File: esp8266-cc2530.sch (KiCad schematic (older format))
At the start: 34 parts, among them J1 CC2530_programmingHeader, U1 WeMos_D1_mini, U2 AMS1117-3.3, U3 CC2530Fxxx, U4 RFX2401C, Y1 32.768kHz, Y2 32MHz

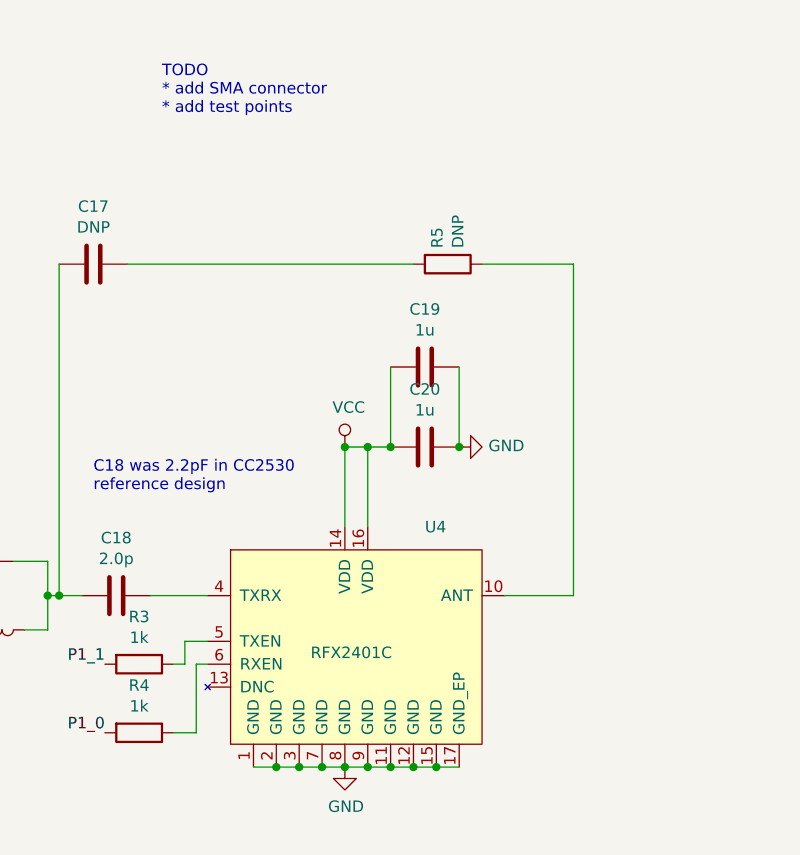
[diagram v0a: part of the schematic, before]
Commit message: added sma connector
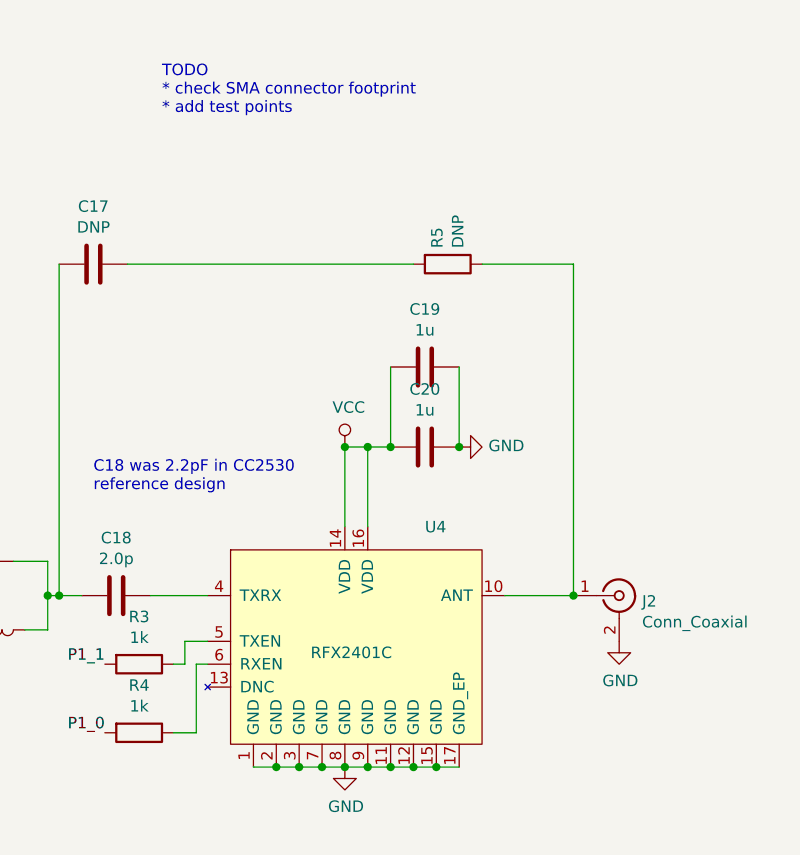
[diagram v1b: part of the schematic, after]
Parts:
- added J2: Conn_Coaxial, Connector_Coaxial:SMA_Amphenol_132289_EdgeMount, symbol Connector:Conn_Coaxial
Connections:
- net GND: now also J2.2 (Ext)
- net at R5.1, U4.10 (ANT): now also J2.1 (In)
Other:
- note added: "TODO\n* check SMA connector footprint\n* add test points"
- note removed: "TODO\n* add SMA connector\n* add test points"
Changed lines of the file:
@@
 Connection ~ 9800 2400
 Text Notes 8500 950  0    50   ~ 0
-TODO\n* add SMA connector\n* add test points
+TODO\n* check SMA connector footprint\n* add test points
 $Comp
 L Device:C C3
@@
 Text Notes 8200 2600 0    50   ~ 0
 C18 was 2.2pF in CC2530 \nreference design
+$Comp
+L Connector:Conn_Coaxial J2
+U 1 1 5ED9BD71
+P 10500 3050
+F 0 "J2" H 10600 3025 50  0000 L CNN
+F 1 "Conn_Coaxial" H 10600 2934 50  0000 L CNN
+F 2 "Connector_Coaxial:SMA_Amphenol_132289_EdgeMount" H 10500 3050 50  0001 C CNN
+F 3 " ~" H 10500 3050 50  0001 C CNN
+	1    10500 3050
+	1    0    0    -1
+$EndComp
+Connection ~ 10300 3050
+$Comp
+L power:GND #PWR0120
+U 1 1 5ED9D9C1
+P 10500 3250
+F 0 "#PWR0120" H 10500 3000 50  0001 C CNN
+F 1 "GND" H 10505 3077 50  0000 C CNN
+F 2 "" H 10500 3250 50  0001 C CNN
+F 3 "" H 10500 3250 50  0001 C CNN
+	1    10500 3250
+	1    0    0    -1
+$EndComp
 $EndSCHEMATC

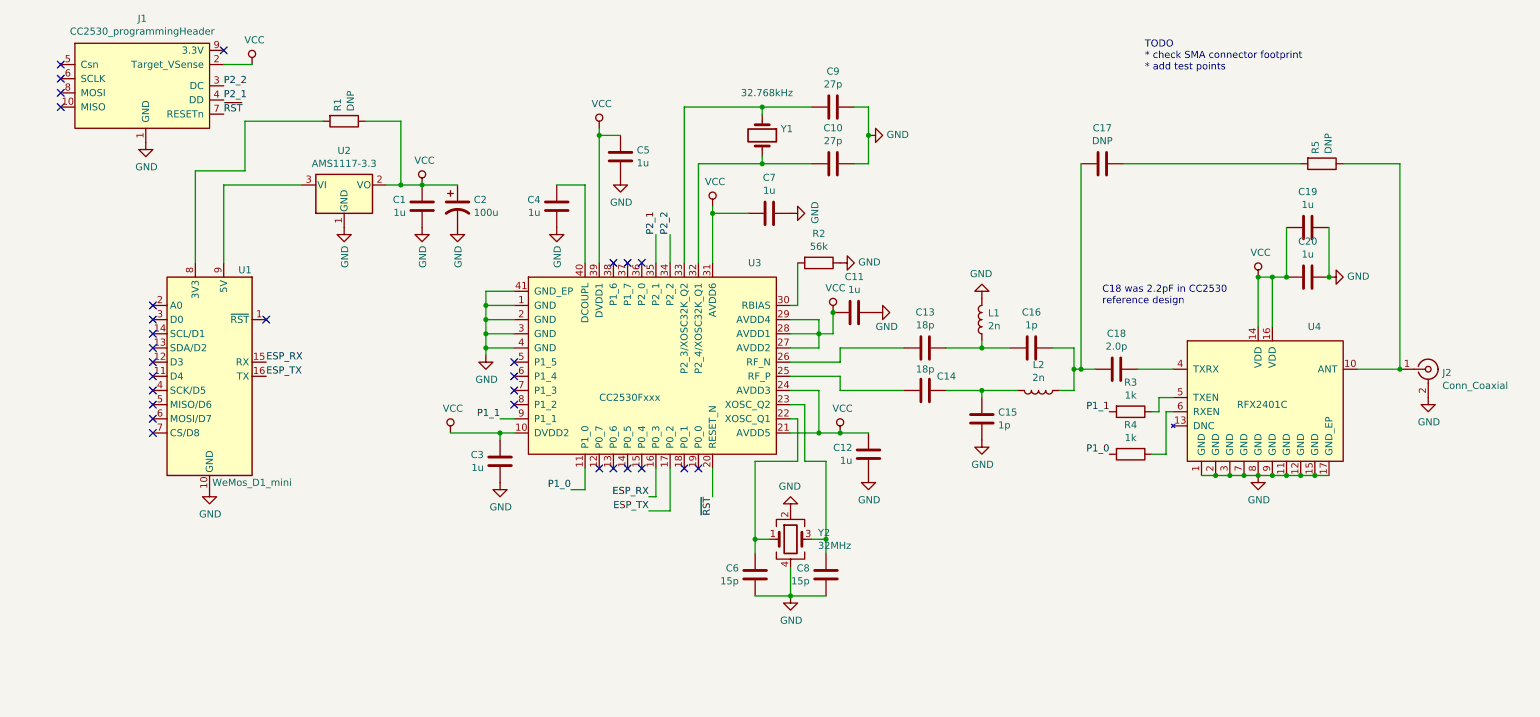
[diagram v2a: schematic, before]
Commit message: removed RFX2401 bypass, added DNP to power CC2530 from debugger
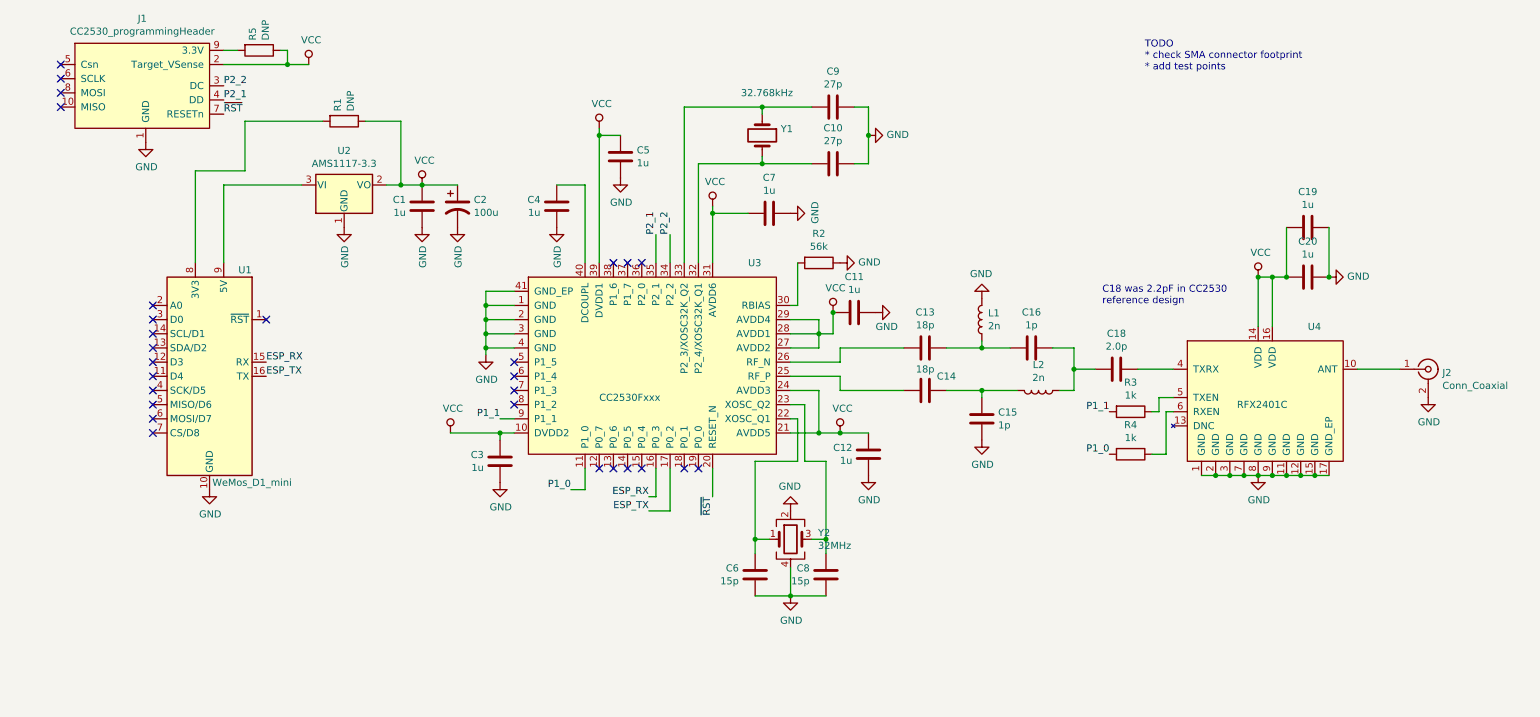
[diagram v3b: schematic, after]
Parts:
- removed C17: DNP, Capacitor_SMD:C_0805_2012Metric, symbol Device:C
- J1: footprint Connector_PinHeader_2.54mm:PinHeader_2x05_P2.54mm_Vertical_SMD -> Connector_PinHeader_1.27mm:PinHeader_2x05_P1.27mm_Vertical_SMD
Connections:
- net VCC: now also R5.1
- net at J2.1 (In), U4.10 (ANT): no longer R5.1
- net at R5.2: now also J1.9 (3.3V)
- no-connect marks 29 -> 28
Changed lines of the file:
@@
 Text Label 5000 3950 2    50   ~ 0
 ESP_RX
-$Comp
-L Device:C C17
-U 1 1 5EB635D2
-P 8200 1600
-F 0 "C17" V 7948 1600 50  0000 C CNN
-F 1 "DNP" V 8039 1600 50  0000 C CNN
-F 2 "Capacitor_SMD:C_0805_2012Metric" H 8238 1450 50  0001 C CNN
-F 3 "~" H 8200 1600 50  0001 C CNN
-	1    8200 1600
-	0    -1   1    0
-$EndComp
-$Comp
-L Device:R R5
-U 1 1 5EB77ED4
-P 9750 1600
-F 0 "R5" H 9680 1554 50  0000 R CNN
-F 1 "DNP" H 9680 1645 50  0000 R CNN
-F 2 "Resistor_SMD:R_0805_2012Metric" V 9680 1600 50  0001 C CNN
-F 3 "~" H 9750 1600 50  0001 C CNN
-	1    9750 1600
-	0    1    1    0
-$EndComp
 Text Label 8250 3350 2    50   ~ 0
 P1_1
 Text Label 8250 3650 2    50   ~ 0
 P1_0
-Wire Wire Line
-	9900 1600 10300 1600
-Wire Wire Line
-	8350 1600 9600 1600
-Wire Wire Line
-	8000 3050 8050 3050
-Wire Wire Line
-	10300 1600 10300 3050
-Wire Wire Line
-	8050 1600 8050 3050
-Connection ~ 8050 3050
-Wire Wire Line
-	8050 3050 8150 3050
 $Comp
 L power:GND #PWR0129
@@
 F 0 "J1" H 1425 1325 50  0000 C CNN
 F 1 "CC2530_programmingHeader" H 1425 1234 50  0000 C CNN
-F 2 "Connector_PinHeader_2.54mm:PinHeader_2x05_P2.54mm_Vertical_SMD" H 2100 750 50  0001 C CNN
+F 2 "Connector_PinHeader_1.27mm:PinHeader_2x05_P1.27mm_Vertical_SMD" H 2100 750 50  0001 C CNN
 F 3 "" H 2100 750 50  0001 C CNN
 F 4 "C124391" H 1200 950 50  0001 C CNN "LCSC"
@@
 L power:VCC #PWR02
 U 1 1 5EBCB7BA
-P 2200 900
-F 0 "#PWR02" H 2200 750 50  0001 C CNN
-F 1 "VCC" H 2217 1073 50  0000 C CNN
-F 2 "" H 2200 900 50  0001 C CNN
-F 3 "" H 2200 900 50  0001 C CNN
-	1    2200 900
-	1    0    0    -1
-$EndComp
-Wire Wire Line
-	2000 900  2200 900
-NoConn ~ 2000 800
+P 2600 900
+F 0 "#PWR02" H 2600 750 50  0001 C CNN
+F 1 "VCC" H 2617 1073 50  0000 C CNN
+F 2 "" H 2600 900 50  0001 C CNN
+F 3 "" H 2600 900 50  0001 C CNN
+	1    2600 900
+	1    0    0    -1
+$EndComp
+Wire Wire Line
+	2000 900  2450 900
 Text Label 2000 1050 0    50   ~ 0
 P2_2
@@
 	1    0    0    -1
 $EndComp
-Connection ~ 10300 3050
 $Comp
 L power:GND #PWR0120
@@
 	1    0    0    1
 $EndComp
+Wire Wire Line
+	8000 3050 8150 3050
+$Comp
+L Device:R R5
+U 1 1 5EAF2D38
+P 2250 800
+F 0 "R5" H 2180 754 50  0000 R CNN
+F 1 "DNP" H 2180 845 50  0000 R CNN
+F 2 "Resistor_SMD:R_0805_2012Metric" V 2180 800 50  0001 C CNN
+F 3 "~" H 2250 800 50  0001 C CNN
+	1    2250 800
+	0    1    1    0
+$EndComp
+Wire Wire Line
+	2100 800  2000 800
+Wire Wire Line
+	2400 800  2450 800
+Wire Wire Line
+	2450 800  2450 900
+Connection ~ 2450 900
+Wire Wire Line
+	2450 900  2600 900
 $EndSCHEMATC

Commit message: fixed SMA connector footprint and added 3d model.
thinking of changing cases... extra board outlines on edge.cuts
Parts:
- J2: footprint Connector_Coaxial:SMA_Amphenol_132289_EdgeMount -> esp8266-cc2530:CON-SMA-EDGE-S(RP)
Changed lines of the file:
@@
 F 0 "J2" H 10600 3025 50  0000 L CNN
 F 1 "Conn_Coaxial" H 10600 2934 50  0000 L CNN
-F 2 "Connector_Coaxial:SMA_Amphenol_132289_EdgeMount" H 10500 3050 50  0001 C CNN
+F 2 "esp8266-cc2530:CON-SMA-EDGE-S(RP)" H 10500 3050 50  0001 C CNN
 F 3 " ~" H 10500 3050 50  0001 C CNN
 	1    10500 3050

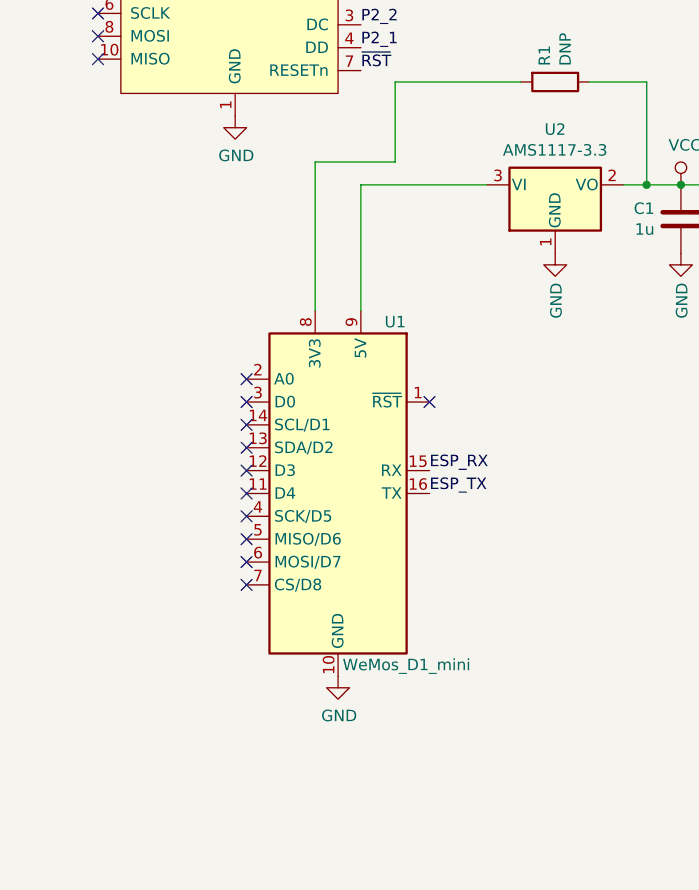
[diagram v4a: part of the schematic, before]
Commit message: updated layout * new WEMOS D1 footprint and 3d model * switched to case TW5-2-5
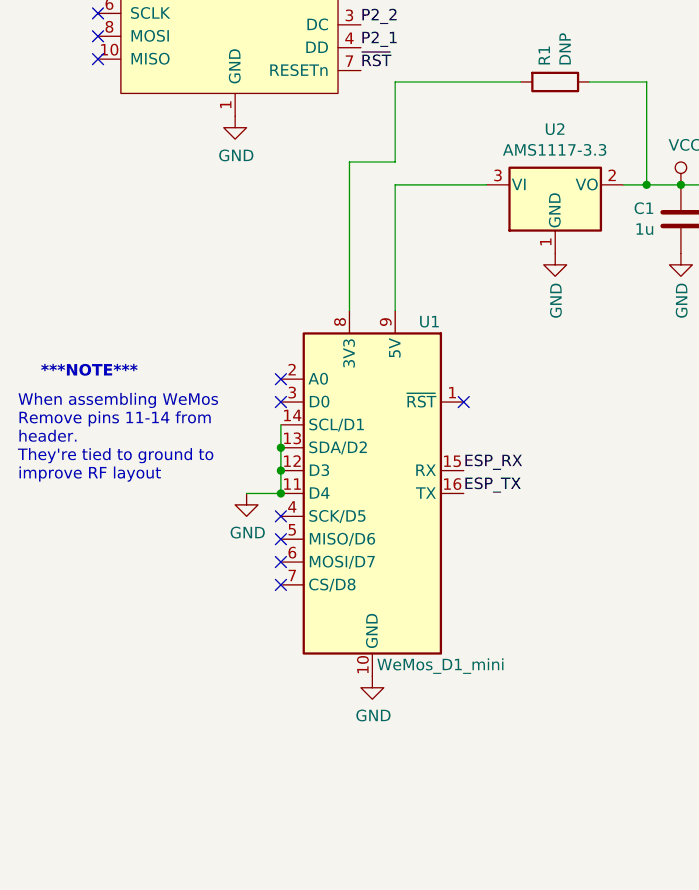
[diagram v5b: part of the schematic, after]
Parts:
- U1: footprint Module:WEMOS_D1_mini_light -> esp8266-cc2530:WEMOS_D1_mini_smt
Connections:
- net GND: now also U1.11 (D4), U1.12 (D3), U1.13 (SDA/D2), U1.14 (SCL/D1)
- no-connect marks 28 -> 24
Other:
- note added: "***NOTE***"
- note added: "When assembling WeMos\nRemove pins 11-14 from \nheader. \nThey're tied to ground to\nimprove RF layout"
- moved on the sheet: U1
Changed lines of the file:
@@
 L power:GND #PWR0129
 U 1 1 5EBADD70
-P 1900 3900
-F 0 "#PWR0129" H 1900 3650 50  0001 C CNN
-F 1 "GND" H 1905 3727 50  0000 C CNN
-F 2 "" H 1900 3900 50  0001 C CNN
-F 3 "" H 1900 3900 50  0001 C CNN
-	1    1900 3900
-	1    0    0    -1
-$EndComp
-Text Label 2300 3000 0    50   ~ 0
+P 2050 3900
+F 0 "#PWR0129" H 2050 3650 50  0001 C CNN
+F 1 "GND" H 2055 3727 50  0000 C CNN
+F 2 "" H 2050 3900 50  0001 C CNN
+F 3 "" H 2050 3900 50  0001 C CNN
+	1    2050 3900
+	1    0    0    -1
+$EndComp
+Text Label 2450 3000 0    50   ~ 0
 ESP_RX
-Text Label 2300 3100 0    50   ~ 0
+Text Label 2450 3100 0    50   ~ 0
 ESP_TX
 $Comp
@@
 $EndComp
 Wire Wire Line
-	2000 1750 2000 2300
+	2150 1750 2150 2300
 Wire Wire Line
 	3000 1300 3250 1300
@@
 L projectLib:WeMos_D1_mini U1
 U 1 1 5EC6ED24
-P 1900 3100
-F 0 "U1" H 1650 3850 50  0000 C CNN
-F 1 "WeMos_D1_mini" H 1600 2350 50  0000 C CNN
-F 2 "Module:WEMOS_D1_mini_light" H 1900 1950 50  0001 C CNN
-F 3 "https://wiki.wemos.cc/products:d1:d1_mini#documentation" H 50  1950 50  0001 C CNN
-	1    1900 3100
+P 2050 3100
+F 0 "U1" H 1800 3850 50  0000 C CNN
+F 1 "WeMos_D1_mini" H 1750 2350 50  0000 C CNN
+F 2 "esp8266-cc2530:WEMOS_D1_mini_smt" H 2050 1950 50  0001 C CNN
+F 3 "https://wiki.wemos.cc/products:d1:d1_mini#documentation" H 200 1950 50  0001 C CNN
+	1    2050 3100
 	-1   0    0    -1
 $EndComp
-NoConn ~ 2300 2700
-NoConn ~ 1500 2600
-NoConn ~ 1500 2700
-NoConn ~ 1500 2800
-NoConn ~ 1500 2900
-NoConn ~ 1500 3000
-NoConn ~ 1500 3100
-NoConn ~ 1500 3200
-NoConn ~ 1500 3300
-NoConn ~ 1500 3400
-NoConn ~ 1500 3500
+NoConn ~ 2450 2700
+NoConn ~ 1650 2600
+NoConn ~ 1650 2700
+NoConn ~ 1650 3200
+NoConn ~ 1650 3300
+NoConn ~ 1650 3400
+NoConn ~ 1650 3500
 NoConn ~ 4750 2300
 NoConn ~ 4850 2300
@@
 NoConn ~ 5350 3750
 Wire Wire Line
-	2000 1750 2550 1750
+	2150 1750 2550 1750
 Wire Wire Line
 	2150 1300 2150 1650
 Wire Wire Line
-	2150 1650 1800 1650
-Wire Wire Line
-	1800 1650 1800 2300
+	2150 1650 1950 1650
+Wire Wire Line
+	1950 1650 1950 2300
 Wire Wire Line
 	2150 1300 2700 1300
@@
 Wire Wire Line
 	2450 900  2600 900
+$Comp
+L power:GND #PWR0121
+U 1 1 5EAE54B3
+P 1500 3100
+F 0 "#PWR0121" H 1500 2850 50  0001 C CNN
+F 1 "GND" H 1505 2927 50  0000 C CNN
+F 2 "" H 1500 3100 50  0001 C CNN
+F 3 "" H 1500 3100 50  0001 C CNN
+	1    1500 3100
+	1    0    0    -1
+$EndComp
+Wire Wire Line
+	1500 3100 1650 3100
+Wire Wire Line
+	1650 2800 1650 2900
+Connection ~ 1650 3100
+Connection ~ 1650 2900
+Wire Wire Line
+	1650 2900 1650 3000
+Connection ~ 1650 3000
+Wire Wire Line
+	1650 3000 1650 3100
+Text Notes 600  2600 0    50   ~ 10
+***NOTE***
+Text Notes 500  3050 0    50   ~ 0
+When assembling WeMos\nRemove pins 11-14 from \nheader.  \nThey're tied to ground to\nimprove RF layout
 $EndSCHEMATC
